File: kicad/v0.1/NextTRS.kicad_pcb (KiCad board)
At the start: 2 copper layers, 63 parts, among them J1 TRS-80 M3 Pin Header, J10 DB15_Female_HighDensity, J2 TRS-80 M1 Pin Connector, J3 TRS-80 M3 Edge Connector, J4 TRS-80 M1 Edge Connector, J5 Programmer, J6 SD_Card, J7 AudioJack3, J8 Mini-DIN-6, J9 USB_B_Micro, Q1 2N7002, Q2 2N7002, Q3 2N7002, Q4 MMBT3904, Q5 MMBT3904, SW1 SW_Push, SW2 ESP_RESET, SW3 PTRS_RESET, SW4 SW_Push, SW5 SW_DIP_x04, U1 ESP32-WROVER-B, U2 74LVC245, U3 74LVC245, U4 74LVC245, U5 74LVC245, U6 74LVC245, U7 MCP43x1

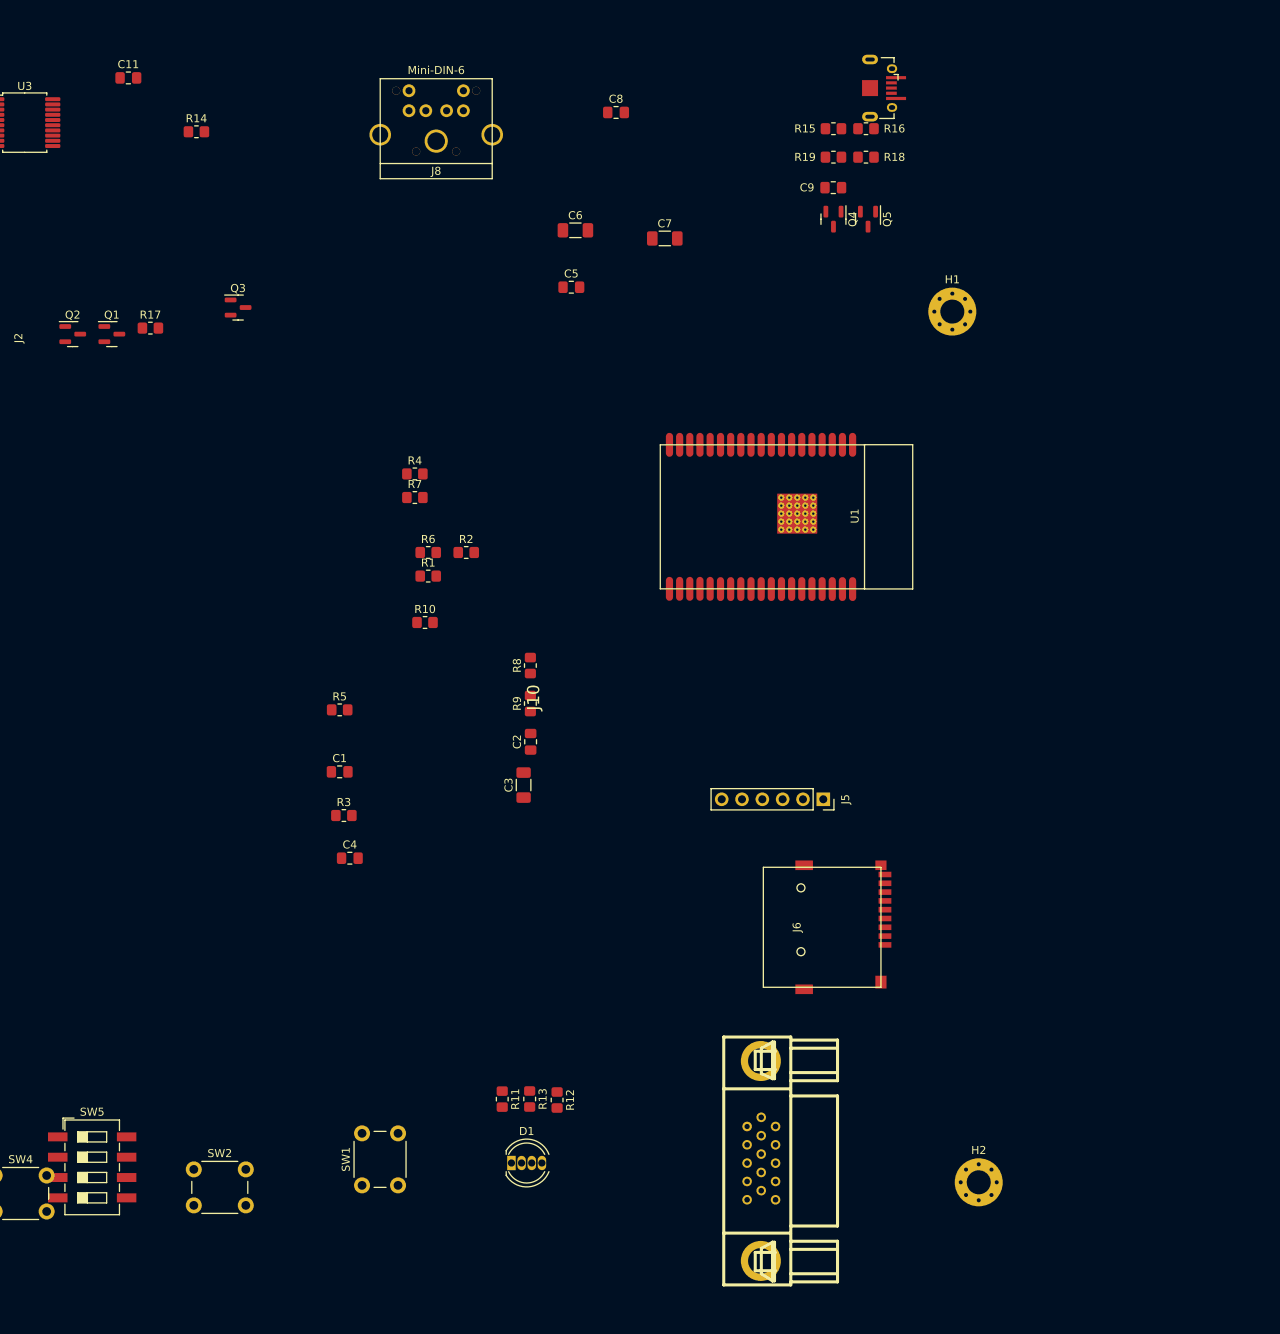
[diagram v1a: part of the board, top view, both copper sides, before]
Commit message: Add hires interface for the M3
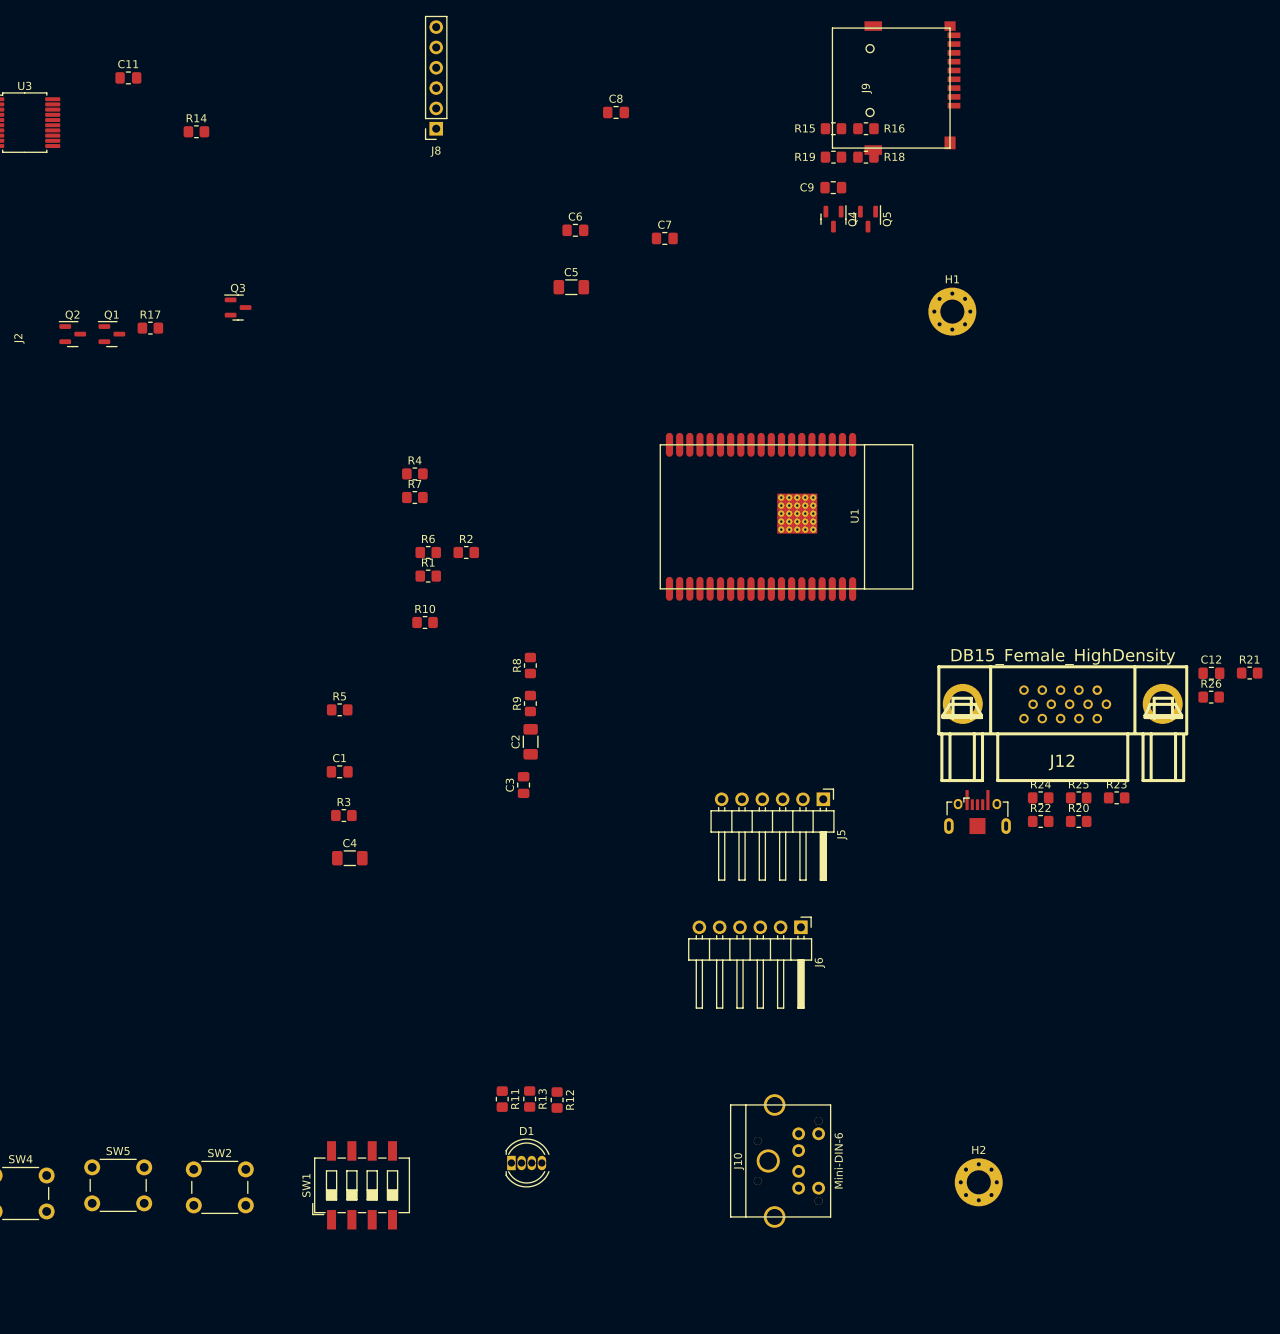
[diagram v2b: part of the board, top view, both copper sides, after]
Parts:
- added C12: 0.1uF, Capacitor_SMD:C_0805_2012Metric_Pad1.18x1.45mm_HandSolder, F.Cu at (305.8, 90.4)
- added J11: USB_B_Micro, PocketTRS_Connectors:USBmicro-B, F.Cu at (276.6, 109.5)
- added J12: DB15_Female_HighDensity, PocketTRS_Connectors:DB_15F-VGA, F.Cu at (287.2, 96.7)
- added R20: 12K, Resistor_SMD:R_0805_2012Metric_Pad1.20x1.40mm_HandSolder, F.Cu at (289.2, 108.9)
- added R21: 4K7, Resistor_SMD:R_0805_2012Metric_Pad1.20x1.40mm_HandSolder, F.Cu at (310.6, 90.4)
- added R22: 4K7, Resistor_SMD:R_0805_2012Metric_Pad1.20x1.40mm_HandSolder, F.Cu at (284.5, 108.9)
- added R23: 4K7, Resistor_SMD:R_0805_2012Metric_Pad1.20x1.40mm_HandSolder, F.Cu at (294.0, 106.0)
- added R24: 2K, Resistor_SMD:R_0805_2012Metric_Pad1.20x1.40mm_HandSolder, F.Cu at (284.5, 106.0)
- added R25: 2K, Resistor_SMD:R_0805_2012Metric_Pad1.20x1.40mm_HandSolder, F.Cu at (289.2, 106.0)
- added R26: 4K7, Resistor_SMD:R_0805_2012Metric_Pad1.20x1.40mm_HandSolder, F.Cu at (305.8, 93.4)
- C1: value 0.1uF -> 100
- C2: value 0.1uF -> 1U; footprint Capacitor_SMD:C_0805_2012Metric_Pad1.18x1.45mm_HandSolder -> Capacitor_SMD:C_1206_3216Metric_Pad1.33x1.80mm_HandSolder
- C3: value 1U -> 100N; footprint Capacitor_SMD:C_1206_3216Metric_Pad1.33x1.80mm_HandSolder -> Capacitor_SMD:C_0805_2012Metric_Pad1.18x1.45mm_HandSolder
- C4: value 100N -> 10U; footprint Capacitor_SMD:C_0805_2012Metric_Pad1.18x1.45mm_HandSolder -> Capacitor_SMD:C_1206_3216Metric_Pad1.33x1.80mm_HandSolder
- C5: value 0.1uF -> 10U; footprint Capacitor_SMD:C_0805_2012Metric_Pad1.18x1.45mm_HandSolder -> Capacitor_SMD:C_1206_3216Metric_Pad1.33x1.80mm_HandSolder
- C6, C7: value 10U -> 0.1uF; footprint Capacitor_SMD:C_1206_3216Metric_Pad1.33x1.80mm_HandSolder -> Capacitor_SMD:C_0805_2012Metric_Pad1.18x1.45mm_HandSolder
- C8: value 100N -> 0.1uF
- C9: value 0.1uF -> 100N
- J10: value DB15_Female_HighDensity -> Mini-DIN-6; footprint PocketTRS_Connectors:DB_15F-VGA -> PocketTRS_Connectors:minidin_6_ps2_pcb_mount
- J5: value Programmer -> Conn_01x06_Male; footprint Connector_PinSocket_2.54mm:PinSocket_1x06_P2.54mm_Vertical -> Connector_PinHeader_2.54mm:PinHeader_1x06_P2.54mm_Horizontal
- J6: value SD_Card -> Conn_01x06_Male; footprint PocketTRS_Connectors:TFP09-2-12B -> Connector_PinHeader_2.54mm:PinHeader_1x06_P2.54mm_Horizontal
- J8: value Mini-DIN-6 -> Programmer; footprint PocketTRS_Connectors:minidin_6_ps2_pcb_mount -> Connector_PinSocket_2.54mm:PinSocket_1x06_P2.54mm_Vertical
- J9: value USB_B_Micro -> SD_Card; footprint PocketTRS_Connectors:USBmicro-B -> PocketTRS_Connectors:TFP09-2-12B
- R10, R15, R16: value 4K7 -> 10K
- R12: value 270R -> 4K7
- R13: value 150R -> 270R
- R14: value 4K7 -> 150R
- R17, R18: value 2K -> 10K
- R19: value 4K7 -> 12K
- R4, R5: value 10K -> 4K7
- R6, R7: value 12K -> 4K7
- SW1: value SW_Push -> SW_DIP_x04; footprint Button_Switch_THT:SW_PUSH_6mm -> Button_Switch_SMD:SW_DIP_SPSTx04_Slide_6.7x11.72mm_W8.61mm_P2.54mm_LowProfile
- SW2: value ESP_RESET -> SW_Push
- SW3: value PTRS_RESET -> ESP_RESET
- SW4: value SW_Push -> PTRS_RESET
- SW5: value SW_DIP_x04 -> SW_Push; footprint Button_Switch_SMD:SW_DIP_SPSTx04_Slide_6.7x11.72mm_W8.61mm_P2.54mm_LowProfile -> Button_Switch_THT:SW_PUSH_6mm
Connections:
- C1 pad 1: GND -> VIDEO_O
- C1 pad 2: +3V3 -> GND
- C2 pad 1: GND -> CASS_IN
- C2 pad 2: +3V3 -> GND
- C3 pad 1: CASS_IN -> Net-(C3-Pad1)
- C4 pad 2: GND -> CASS_IN
- C5 pad 1: GND -> Net-(C5-Pad1)
- C5 pad 2: +3V3 -> Net-(C3-Pad1)
- C6 pad 1: Net-(C6-Pad1) -> GND
- C6 pad 2: CASS_IN -> +3V3
- C7 pad 1: Net-(C7-Pad1) -> GND
- C7 pad 2: Net-(C4-Pad1) -> +3V3
- C8 pad 1: ESP_RESET -> GND
- C8 pad 2: GND -> +3V3
- C9 pad 1: GND -> ESP_RESET
- C9 pad 2: +3V3 -> GND
- Conn1 pad 143: unconnected-(Conn1-Pad143) -> CONF_4
- Conn1 pad 147: unconnected-(Conn1-Pad147) -> CONF_3
- Conn1 pad 149: unconnected-(Conn1-Pad149) -> CONF_2
- Conn1 pad 153: unconnected-(Conn1-Pad153) -> CONF_1
- Conn1 pad 183: unconnected-(Conn1-Pad183) -> HSYNC_O
- Conn1 pad 191: unconnected-(Conn1-Pad191) -> VSYNC_O
- Conn1 pad 192: CONF_1 -> HSYNCX
- Conn1 pad 193: unconnected-(Conn1-Pad193) -> VIDEO_O
- Conn1 pad 194: CONF_2 -> VSYNCX
- Conn1 pad 198: CONF_3 -> VIDEOX
- Conn1 pad 200: CONF_4 -> unconnected-(Conn1-Pad200)
- J10 pad 1: POT_VGA_RED -> PS2_DATA
- J10 pad 2: POT_VGA_GREEN -> unconnected-(J10-Pad2)
- J10 pad 3: POT_VGA_BLUE -> GND
- J10 pad 4: unconnected-(J10-Pad4) -> +5V
- J10 pad 5: GND -> PS2_CLK
- J10 pad 6: GND -> unconnected-(J10-Pad6)
- J5 pad 1: Net-(J5-Pad1) -> GND
- J5 pad 2: Net-(J5-Pad2) -> VIDEO
- J5 pad 3: TXD0 -> GND
- J5 pad 4: RXD0 -> VSYNC
- J5 pad 5: +5V -> GND
- J5 pad 6: GND -> HSYNC
- J6 pad 1: Net-(J6-Pad1) -> GND
- J6 pad 2: CS_SD -> VIDEO_O
- J6 pad 3: MOSI -> GND
- J6 pad 4: +3.3V -> VSYNC_O
- J6 pad 5: SCK -> GND
- J6 pad 6: GND -> HSYNC_O
- J7 pad R: Net-(C6-Pad1) -> Net-(C4-Pad1)
- J7 pad T: Net-(C7-Pad1) -> Net-(C5-Pad1)
- J8 pad 1: PS2_DATA -> Net-(J8-Pad1)
- J8 pad 2: unconnected-(J8-Pad2) -> Net-(J8-Pad2)
- J8 pad 3: GND -> TXD0
- J8 pad 4: +5V -> RXD0
- J8 pad 5: PS2_CLK -> +5V
- J8 pad 6: unconnected-(J8-Pad6) -> GND
- J9 pad 1: +5V -> Net-(J9-Pad1)
- J9 pad 2: unconnected-(J9-Pad2) -> CS_SD
- J9 pad 3: unconnected-(J9-Pad3) -> MOSI
- J9 pad 4: unconnected-(J9-Pad4) -> +3.3V
- J9 pad 5: GND -> SCK
- Q4 pad 2: Net-(J5-Pad1) -> Net-(J8-Pad1)
- Q5 pad 2: Net-(J5-Pad2) -> Net-(J8-Pad2)
- R10 pad 1: +3.3V -> VIDEO
- R10 pad 2: CASS_IN -> GND
- R11 pad 1: CASS_IN -> +3.3V
- R11 pad 2: GND -> CASS_IN
- R12 pad 1: Net-(C4-Pad1) -> CASS_IN
- R12 pad 2: CASS_OUT -> GND
- R13 pad 1: Net-(C4-Pad1) -> Net-(C3-Pad1)
- R13 pad 2: GND -> CASS_OUT
- R14 pad 1: +3V3 -> Net-(C3-Pad1)
- R14 pad 2: I00 -> GND
- R15 pad 1: +3V3 -> +3.3V
- R15 pad 2: ESP_RESET -> MOSI
- R16 pad 1: +3V3 -> +3.3V
- R16 pad 2: PTRS_RESET -> Net-(J9-Pad8)
- R17 pad 1: PS2_CLK -> +3.3V
- R17 pad 2: +3.3V -> CS_SD
- R18 pad 1: PS2_DATA -> +3.3V
- R18 pad 2: +3.3V -> Net-(J9-Pad1)
- R19 pad 1: +3.3V -> Net-(Q4-Pad1)
- R19 pad 2: BUTTON -> Net-(J8-Pad2)
- R4 pad 2: MOSI -> CONF_1
- R5 pad 2: Net-(J6-Pad8) -> CONF_2
- R6 pad 1: Net-(Q4-Pad1) -> +3.3V
- R6 pad 2: Net-(J5-Pad2) -> CONF_3
- R7 pad 1: Net-(Q5-Pad1) -> +3.3V
- R7 pad 2: Net-(J5-Pad1) -> CONF_4
- R8 pad 1: +3.3V -> HSYNC
- R8 pad 2: CS_SD -> GND
- R9 pad 1: +3.3V -> VSYNC
- R9 pad 2: Net-(J6-Pad1) -> GND
- SW1 pad 2: BUTTON -> GND
- SW2 pad 1: ESP_RESET -> GND
- SW2 pad 2: GND -> BUTTON
- SW3 pad 1: GND -> ESP_RESET
- SW3 pad 2: PTRS_RESET -> GND
- SW4 pad 2: BUTTON -> PTRS_RESET
- SW5 pad 2: GND -> BUTTON
- U5 pad 13: unconnected-(U5-Pad13) -> VIDEOX
- U5 pad 14: unconnected-(U5-Pad14) -> VSYNCX
- U5 pad 15: unconnected-(U5-Pad15) -> HSYNCX
- U5 pad 5: unconnected-(U5-Pad5) -> HSYNC
- U5 pad 6: unconnected-(U5-Pad6) -> VSYNC
- U5 pad 7: unconnected-(U5-Pad7) -> VIDEO

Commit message: Add HDMI connector
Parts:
- removed SW4: PTRS_RESET, Button_Switch_THT:SW_PUSH_6mm
- removed SW5: SW_Push, Button_Switch_THT:SW_PUSH_6mm
- removed U7: MCP43x1, Package_SO:TSSOP-20_4.4x6.5mm_P0.65mm
- added C13: 100N, Capacitor_SMD:C_0805_2012Metric_Pad1.18x1.45mm_HandSolder, F.Cu at (78.6, 181.7)
- added C14: 10U, Capacitor_SMD:C_1206_3216Metric_Pad1.33x1.80mm_HandSolder, F.Cu at (79.2, 175.5)
- added C15: 10U, Capacitor_SMD:C_1206_3216Metric_Pad1.33x1.80mm_HandSolder, F.Cu at (79.2, 172.2)
- added C16: 0.1uF, Capacitor_SMD:C_0805_2012Metric_Pad1.18x1.45mm_HandSolder, F.Cu at (84.6, 175.3)
- added C17: 100N, Capacitor_SMD:C_0805_2012Metric_Pad1.18x1.45mm_HandSolder, F.Cu at (78.6, 178.7)
- added C18: 0.1uF, Capacitor_SMD:C_0805_2012Metric_Pad1.18x1.45mm_HandSolder, F.Cu at (83.4, 178.7)
- added C19: 0.1uF, Capacitor_SMD:C_0805_2012Metric_Pad1.18x1.45mm_HandSolder, F.Cu at (90.6, 172.0)
- added R27: 4K7, Resistor_SMD:R_0805_2012Metric_Pad1.20x1.40mm_HandSolder, F.Cu at (35.2, 127.7)
- added R28: 4K7, Resistor_SMD:R_0805_2012Metric_Pad1.20x1.40mm_HandSolder, F.Cu at (33.0, 127.7)
- added R29: 4K7, Resistor_SMD:R_0805_2012Metric_Pad1.20x1.40mm_HandSolder, F.Cu at (30.9, 127.7)
- added R30: 4K7, Resistor_SMD:R_0805_2012Metric_Pad1.20x1.40mm_HandSolder, F.Cu at (88.1, 181.7)
- added R31: 2K, Resistor_SMD:R_0805_2012Metric_Pad1.20x1.40mm_HandSolder, F.Cu at (95.4, 172.0)
- added R32: 2K, Resistor_SMD:R_0805_2012Metric_Pad1.20x1.40mm_HandSolder, F.Cu at (88.2, 178.3)
- added R33: 4K7, Resistor_SMD:R_0805_2012Metric_Pad1.20x1.40mm_HandSolder, F.Cu at (94.1, 175.0)
- added R34: 4K7, Resistor_SMD:R_0805_2012Metric_Pad1.20x1.40mm_HandSolder, F.Cu at (94.1, 177.9)
- added R35: 4K7, Resistor_SMD:R_0805_2012Metric_Pad1.20x1.40mm_HandSolder, F.Cu at (89.4, 175.3)
- added R36: 4K7, Resistor_SMD:R_0805_2012Metric_Pad1.20x1.40mm_HandSolder, F.Cu at (83.4, 181.7)
- C1: value 100 -> 100n
- C12: value 0.1uF -> 1U; footprint Capacitor_SMD:C_0805_2012Metric_Pad1.18x1.45mm_HandSolder -> Capacitor_SMD:C_1206_3216Metric_Pad1.33x1.80mm_HandSolder
- C2: value 1U -> 100n; footprint Capacitor_SMD:C_1206_3216Metric_Pad1.33x1.80mm_HandSolder -> Capacitor_SMD:C_0805_2012Metric_Pad1.18x1.45mm_HandSolder
- C3: value 100N -> 100n
- C4, C5: value 10U -> 100n; footprint Capacitor_SMD:C_1206_3216Metric_Pad1.33x1.80mm_HandSolder -> Capacitor_SMD:C_0805_2012Metric_Pad1.18x1.45mm_HandSolder
- C6, C7, C8: value 0.1uF -> 100n
- C9: value 100N -> 100
- D1: value LED_RCBG -> LED_RKBG
- J1: footprint Connector_PinSocket_2.54mm:PinSocket_2x25_P2.54mm_Vertical -> Connector_PinHeader_2.54mm:PinHeader_2x25_P2.54mm_Vertical
- J10: value Mini-DIN-6 -> AudioJack3; footprint PocketTRS_Connectors:minidin_6_ps2_pcb_mount -> PocketTRS_Connectors:Jack_3.5mm_CUI_SJ1-3535NG_Horizontal_CircularHoles
- J11: value USB_B_Micro -> Mini-DIN-6; footprint PocketTRS_Connectors:USBmicro-B -> PocketTRS_Connectors:minidin_6_ps2_pcb_mount
- J12: value DB15_Female_HighDensity -> USB_B_Micro; footprint PocketTRS_Connectors:DB_15F-VGA -> PocketTRS_Connectors:USBmicro-B
- J2: footprint Connector_PinSocket_2.54mm:PinSocket_2x20_P2.54mm_Vertical -> Connector_PinHeader_2.54mm:PinHeader_2x20_P2.54mm_Vertical
- J7: value AudioJack3 -> HDMI_A; footprint PocketTRS_Connectors:Jack_3.5mm_CUI_SJ1-3535NG_Horizontal_CircularHoles -> Connector_HDMI:HDMI_A_Molex_208658-1001_Horizontal
- Q1, Q2: value 2N7002 -> MMBT3904
- Q4, Q5: value MMBT3904 -> 2N7002
- R10, R8, R9: value 10K -> 50
- R11, R4, R5, R6, R7: value 4K7 -> 50
- R12: value 4K7 -> 10K
- R13: value 270R -> 10K
- R14: value 150R -> 10K
- R23: value 4K7 -> 270R
- R24: value 2K -> 150R
- R25: value 2K -> 4K7
- SW1: value SW_DIP_x04 -> ESP_RESET; footprint Button_Switch_SMD:SW_DIP_SPSTx04_Slide_6.7x11.72mm_W8.61mm_P2.54mm_LowProfile -> Button_Switch_THT:SW_PUSH_6mm
- SW2: value SW_Push -> PTRS_RESET
- SW3: value ESP_RESET -> SW_DIP_x04; footprint Button_Switch_THT:SW_PUSH_6mm -> Button_Switch_SMD:SW_DIP_SPSTx04_Slide_6.7x11.72mm_W8.61mm_P2.54mm_LowProfile
- moved C1 241.8 mm to (-42.1, 139.5)
- moved C12 235.3 mm to (85.2, 172.2)
- moved J1 184.9 mm to (-4.52, 46.8), turned to 90 degrees
- moved U3 165.2 mm to (5.54, 86.5)
- moved J3 159.5 mm to (34.2, 35.0), turned to 180 degrees
- moved U2 139.5 mm to (5.23, 97.4)
- moved U4 108.2 mm to (32.6, 88.1)
- moved J6 107.2 mm to (155.3, 162.9)
- moved R17 102.1 mm to (274.2, 32.7), turned to 90 degrees
- moved J5 100.6 mm to (174.1, 162.8)
- moved R8 85.9 mm to (136.1, 74.3)
- moved R9 84.6 mm to (138.5, 74.3)
- moved U1 83.2 mm to (188.5, 110.1)
- moved R10 79.9 mm to (171.5, 155.4), turned to 90 degrees
- moved C2 79.9 mm to (144.3, 75.9)
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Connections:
- C1 pad 1: VIDEO_O -> HDMI_TX2_P
- C1 pad 2: GND -> Net-(J7-Pad1)
- C12 pad 1: GND -> CASS_IN
- C12 pad 2: +3V3 -> GND
- C2 pad 1: CASS_IN -> HDMI_TX2_N
- C2 pad 2: GND -> Net-(J7-Pad3)
- C3 pad 1: Net-(C3-Pad1) -> HDMI_TX1_P
- C3 pad 2: GND -> Net-(J7-Pad4)
- C4 pad 1: Net-(C4-Pad1) -> HDMI_TX1_N
- C4 pad 2: CASS_IN -> Net-(J7-Pad6)
- C5 pad 1: Net-(C5-Pad1) -> HDMI_TX0_P
- C5 pad 2: Net-(C3-Pad1) -> Net-(J7-Pad7)
- C6 pad 1: GND -> HDMI_TX0_N
- C6 pad 2: +3V3 -> Net-(J7-Pad9)
- C7 pad 1: GND -> HDMI_TXC_P
- C7 pad 2: +3V3 -> Net-(J7-Pad10)
- C8 pad 1: GND -> HDMI_TXC_N
- C8 pad 2: +3V3 -> Net-(J7-Pad12)
- C9 pad 1: ESP_RESET -> VIDEO_O
- Conn1 pad 101: DBUS_DIR -> _D2
- Conn1 pad 103: unconnected-(Conn1-Pad103) -> _D1
- Conn1 pad 107: _RAS_N -> _D0
- Conn1 pad 109: _OUT_N -> unconnected-(Conn1-Pad109)
- Conn1 pad 113: _IN_N -> unconnected-(Conn1-Pad113)
- Conn1 pad 115: _RD_N -> unconnected-(Conn1-Pad115)
- Conn1 pad 119: _WR_N -> unconnected-(Conn1-Pad119)
- Conn1 pad 121: _IOREQ_N -> unconnected-(Conn1-Pad121)
- Conn1 pad 123: _M1_N -> unconnected-(Conn1-Pad123)
- Conn1 pad 125: _RESET_N -> unconnected-(Conn1-Pad125)
- Conn1 pad 130: unconnected-(Conn1-Pad130) -> DONE
- Conn1 pad 135: unconnected-(Conn1-Pad135) -> CASS_OUT
- Conn1 pad 140: EXTIOSEL -> unconnected-(Conn1-Pad140)
- Conn1 pad 142: WAIT -> unconnected-(Conn1-Pad142)
- Conn1 pad 146: INT -> unconnected-(Conn1-Pad146)
- Conn1 pad 148: CTRL_DIR -> unconnected-(Conn1-Pad148)
- Conn1 pad 152: CTRL_EN -> unconnected-(Conn1-Pad152)
- Conn1 pad 154: CTRL1_EN -> EXTIOSEL
- Conn1 pad 176: EXTIOSEL_OUT_N -> WAIT
- Conn1 pad 177: unconnected-(Conn1-Pad177) -> HSYNC_O
- Conn1 pad 180: WAIT_OUT_N -> INT
- Conn1 pad 182: INT_OUT_N -> CTRL1_EN
- Conn1 pad 183: HSYNC_O -> VSYNC_O
- Conn1 pad 186: unconnected-(Conn1-Pad186) -> EXTIOSEL_IN_N
- Conn1 pad 191: VSYNC_O -> VIDEO_O
- Conn1 pad 192: HSYNCX -> WAIT_IN_N
- Conn1 pad 193: VIDEO_O -> VIDEOX
- Conn1 pad 194: VSYNCX -> INT_IN_N
- Conn1 pad 198: VIDEOX -> HSYNCX
- Conn1 pad 200: unconnected-(Conn1-Pad200) -> VSYNCX
- Conn1 pad 26: unconnected-(Conn1-Pad26) -> GND
- Conn1 pad 27: _A0 -> CTRL_DIR
- Conn1 pad 28: VGA_RED -> ABUS_DIR_N
- Conn1 pad 29: _A1 -> CTRL_EN
- Conn1 pad 30: VGA_GREEN -> _A10
- Conn1 pad 33: _A2 -> _RD_N
- Conn1 pad 34: VGA_BLUE -> _A12
- Conn1 pad 35: _A3 -> _WR_N
- Conn1 pad 36: VGA_VSYNC -> _A13
- Conn1 pad 39: _A4 -> _RAS_N
- Conn1 pad 40: VGA_HSYNC -> _A15
- Conn1 pad 41: _A5 -> _IOREQ_N
- Conn1 pad 42: CS_FPGA -> _A14
- Conn1 pad 44: SCK -> _A11
- Conn1 pad 45: _A6 -> _M1_N
- Conn1 pad 46: MISO -> _A8
- Conn1 pad 47: _A7 -> _RESET_N
- Conn1 pad 50: MOSI -> HDMI_TX2_N
- Conn1 pad 51: _A8 -> _OUT_N
- Conn1 pad 52: ESP_S0 -> HDMI_TX2_P
- Conn1 pad 53: _A9 -> _IN_N
- Conn1 pad 56: ESP_S1 -> HDMI_TX1_N
- Conn1 pad 57: _A10 -> ABUS_DIR
- Conn1 pad 58: ESP_S2 -> HDMI_TX1_P
- Conn1 pad 59: _A11 -> ABUS_EN
- Conn1 pad 62: ESP_S3 -> HDMI_TX0_N
- Conn1 pad 63: _A12 -> _A7
- Conn1 pad 64: REQ -> HDMI_TX0_P
- Conn1 pad 65: _A13 -> _A6
- Conn1 pad 67: _A14 -> _A5
- Conn1 pad 68: DONE -> HDMI_TXC_P
- Conn1 pad 69: _A15 -> _A4
- Conn1 pad 70: CASS_OUT -> HDMI_TXC_N
- Conn1 pad 73: ABUS_EN -> _A3
- Conn1 pad 74: unconnected-(Conn1-Pad74) -> _A9
- Conn1 pad 75: ABUS_DIR -> _A2
- Conn1 pad 76: unconnected-(Conn1-Pad76) -> CS_FPGA
- Conn1 pad 77: _D0 -> _A1
- Conn1 pad 78: unconnected-(Conn1-Pad78) -> SCK
- Conn1 pad 79: _D1 -> _A0
- Conn1 pad 80: unconnected-(Conn1-Pad80) -> MISO
- Conn1 pad 81: _D2 -> DBUS_DIR
- Conn1 pad 83: _D3 -> DBUS_EN
- Conn1 pad 84: unconnected-(Conn1-Pad84) -> MOSI
- Conn1 pad 85: _D4 -> _D7
- Conn1 pad 86: unconnected-(Conn1-Pad86) -> ESP_S0
- Conn1 pad 89: _D5 -> _D6
- Conn1 pad 90: unconnected-(Conn1-Pad90) -> ESP_S1
- Conn1 pad 91: _D6 -> _D5
- Conn1 pad 92: unconnected-(Conn1-Pad92) -> ESP_S2
- Conn1 pad 95: _D7 -> _D4
- Conn1 pad 96: unconnected-(Conn1-Pad96) -> ESP_S3
- Conn1 pad 97: DBUS_EN -> _D3
- Conn1 pad 98: unconnected-(Conn1-Pad98) -> REQ
- J11 pad 1: +5V -> PS2_DATA
- J11 pad 3: unconnected-(J11-Pad3) -> GND
- J11 pad 4: unconnected-(J11-Pad4) -> +5V
- J11 pad 5: GND -> PS2_CLK
- J12 pad 1: POT_VGA_RED -> +5V
- J12 pad 2: POT_VGA_GREEN -> unconnected-(J12-Pad2)
- J12 pad 3: POT_VGA_BLUE -> unconnected-(J12-Pad3)
- Q1 pad 1: INT -> Net-(Q1-Pad1)
- Q1 pad 2: GND -> Net-(J8-Pad1)
- Q1 pad 3: INT_N -> ESP_RESET
- Q2 pad 1: WAIT -> Net-(Q2-Pad1)
- Q2 pad 2: GND -> Net-(J8-Pad2)
- Q2 pad 3: WAIT_N -> I00
- Q3 pad 1: EXTIOSEL -> INT
- Q3 pad 3: EXTIOSEL_N -> INT_N
- Q4 pad 1: Net-(Q4-Pad1) -> WAIT
- Q4 pad 2: Net-(J8-Pad1) -> GND
- Q4 pad 3: ESP_RESET -> WAIT_N
- Q5 pad 1: Net-(Q5-Pad1) -> EXTIOSEL
- Q5 pad 2: Net-(J8-Pad2) -> GND
- Q5 pad 3: I00 -> EXTIOSEL_N
- R10 pad 1: VIDEO -> +3.3V
- R10 pad 2: GND -> HDMI_TXC_P
- R11 pad 2: CASS_IN -> HDMI_TXC_N
- R12 pad 1: CASS_IN -> HSYNC
- R13 pad 1: Net-(C3-Pad1) -> VSYNC
- R13 pad 2: CASS_OUT -> GND
- R14 pad 1: Net-(C3-Pad1) -> VIDEO
- R19 pad 1: Net-(Q4-Pad1) -> Net-(Q1-Pad1)
- R20 pad 1: Net-(Q5-Pad1) -> Net-(Q2-Pad1)
- R21 pad 1: +3V3 -> +3.3V
- R21 pad 2: I00 -> CASS_IN
- R22 pad 1: +3V3 -> CASS_IN
- R22 pad 2: ESP_RESET -> GND
- R23 pad 1: +3V3 -> Net-(C13-Pad1)
- R23 pad 2: PTRS_RESET -> CASS_OUT
- R24 pad 1: PS2_CLK -> Net-(C13-Pad1)
- R24 pad 2: +3.3V -> GND
- R25 pad 1: PS2_DATA -> +3.3V
- R25 pad 2: +3.3V -> I00
- R26 pad 1: +3.3V -> +3V3
- R26 pad 2: BUTTON -> INT_IN_N
- R4 pad 2: CONF_1 -> HDMI_TX2_P
- R5 pad 2: CONF_2 -> HDMI_TX2_N
- R6 pad 2: CONF_3 -> HDMI_TX1_P
- R7 pad 2: CONF_4 -> HDMI_TX1_N
- R8 pad 1: HSYNC -> +3.3V
- R8 pad 2: GND -> HDMI_TX0_P
- R9 pad 1: VSYNC -> +3.3V
- R9 pad 2: GND -> HDMI_TX0_N
- SW1 pad 1: GND -> ESP_RESET
- SW3 pad 1: ESP_RESET -> GND
- U1 pad 26: CS43x1 -> unconnected-(U1-Pad26)
- U1 pad 5: BUTTON -> unconnected-(U1-Pad5)
- U1 pad 7: PTRS_RESET -> BUTTON
- U2 pad 11: _A7 -> _A0
- U2 pad 12: _A6 -> _A1
- U2 pad 13: _A5 -> _A2
- U2 pad 14: _A4 -> _A3
- U2 pad 15: _A3 -> _A4
- U2 pad 16: _A2 -> _A5
- U2 pad 17: _A1 -> _A6
- U2 pad 18: _A0 -> _A7
- U2 pad 2: A0 -> A7
- U2 pad 3: A1 -> A6
- U2 pad 4: A2 -> A5
- U2 pad 5: A3 -> A4
- U2 pad 6: A4 -> A3
- U2 pad 7: A5 -> A2
- U2 pad 8: A6 -> A1
- U2 pad 9: A7 -> A0
- U3 pad 11: _RESET_N -> _IN_N
- U3 pad 12: _M1_N -> _OUT_N
- U3 pad 13: _IOREQ_N -> _RESET_N
- U3 pad 14: _WR_N -> _M1_N
- U3 pad 15: _RD_N -> _IOREQ_N
- U3 pad 16: _IN_N -> _RAS_N
- U3 pad 17: _OUT_N -> _WR_N
- U3 pad 18: _RAS_N -> _RD_N
- U3 pad 2: RAS_N -> RD_N
- U3 pad 3: OUT_N -> WR_N
- U3 pad 4: IN_N -> RAS_N
- U3 pad 5: RD_N -> IOREQ_N
- U3 pad 6: WR_N -> M1_N
- U3 pad 7: IOREQ_N -> RESET_N
- U3 pad 8: M1_N -> OUT_N
- U3 pad 9: RESET_N -> IN_N
- U4 pad 1: ABUS_DIR -> ABUS_DIR_N
- U4 pad 11: _A15 -> A9
- U4 pad 12: _A14 -> A8
- U4 pad 13: _A13 -> A11
- U4 pad 14: _A12 -> A14
- U4 pad 15: _A11 -> A15
- U4 pad 16: _A10 -> A13
- U4 pad 17: _A9 -> A12
- U4 pad 18: _A8 -> A10
- U4 pad 2: A8 -> _A10
- U4 pad 3: A9 -> _A12
- U4 pad 4: A10 -> _A13
- U4 pad 5: A11 -> _A15
- U4 pad 6: A12 -> _A14
- U4 pad 7: A13 -> _A11
- U4 pad 8: A14 -> _A8
- U4 pad 9: A15 -> _A9
- U5 pad 1: +3V3 -> GND
- U5 pad 2: EXTIOSEL_OUT_N -> EXTIOSEL_IN_N
- U5 pad 3: WAIT_OUT_N -> WAIT_IN_N
- U5 pad 4: INT_OUT_N -> INT_IN_N
- U6 pad 11: _D7 -> _D0
- U6 pad 12: _D6 -> _D1
- U6 pad 13: _D5 -> _D2
- U6 pad 14: _D4 -> _D3
- U6 pad 15: _D3 -> _D4
- U6 pad 16: _D2 -> _D5
- U6 pad 17: _D1 -> _D6
- U6 pad 18: _D0 -> _D7
- U6 pad 2: D0 -> D7
- U6 pad 3: D1 -> D6
- U6 pad 4: D2 -> D5
- U6 pad 5: D3 -> D4
- U6 pad 6: D4 -> D3
- U6 pad 7: D5 -> D2
- U6 pad 8: D6 -> D1
- U6 pad 9: D7 -> D0

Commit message: Move LED to FPGA. Add JTAG interface
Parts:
- SW2: value PTRS_RESET -> PTRS_RESET/STATUS
- moved J12 272.2 mm to (15.6, 79.2), turned to -90 degrees
- moved H1 248.1 mm to (25.8, 60.5)
- moved R26 239.4 mm to (70.8, 139.0)
- moved C9 235.4 mm to (61.6, 158.6), turned to 0 degrees
- moved R27 228.9 mm to (256.3, 68.7), turned to 0 degrees
- moved H3 223.5 mm to (161.8, 169.0)
- moved SW2 214.1 mm to (24.0, 142.9)
- moved C17 205.1 mm to (246.3, 60.7)
- moved C1 187.5 mm to (139.4, 92.8)
- moved Q5 179.8 mm to (88.5, 77.4), turned to 0 degrees
- moved SW3 177.5 mm to (27.1, 132.3)
- moved SW1 175.8 mm to (23.8, 153.6), turned to 0 degrees
- moved R21 172.9 mm to (148.0, 149.3)
- moved R14 166.2 mm to (82.0, 157.8)
- moved R23 160.2 mm to (141.1, 153.9)
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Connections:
- C1 pad 2: Net-(J7-Pad1) -> Net-(C1-Pad2)
- C2 pad 2: Net-(J7-Pad3) -> Net-(C2-Pad2)
- C3 pad 2: Net-(J7-Pad4) -> Net-(C3-Pad2)
- C4 pad 2: Net-(J7-Pad6) -> Net-(C4-Pad2)
- C5 pad 2: Net-(J7-Pad7) -> Net-(C5-Pad2)
- C6 pad 2: Net-(J7-Pad9) -> Net-(C6-Pad2)
- C7 pad 2: Net-(J7-Pad10) -> Net-(C7-Pad2)
- C8 pad 2: Net-(J7-Pad12) -> Net-(C8-Pad2)
- Conn1 pad 123: unconnected-(Conn1-Pad123) -> CONF_4
- Conn1 pad 125: unconnected-(Conn1-Pad125) -> CONF_3
- Conn1 pad 129: unconnected-(Conn1-Pad129) -> CONF_2
- Conn1 pad 131: unconnected-(Conn1-Pad131) -> CONF_1
- Conn1 pad 140: unconnected-(Conn1-Pad140) -> LED_GREEN
- Conn1 pad 142: unconnected-(Conn1-Pad142) -> LED_BLUE
- Conn1 pad 143: CONF_4 -> JTAG_TMS
- Conn1 pad 146: unconnected-(Conn1-Pad146) -> LED_RED
- Conn1 pad 147: CONF_3 -> RXD0
- Conn1 pad 149: CONF_2 -> JTAG_TCK
- Conn1 pad 153: CONF_1 -> TXD0
- J7 pad 1: Net-(J7-Pad1) -> Net-(C1-Pad2)
- J7 pad 10: Net-(J7-Pad10) -> Net-(C7-Pad2)
- J7 pad 12: Net-(J7-Pad12) -> Net-(C8-Pad2)
- J7 pad 3: Net-(J7-Pad3) -> Net-(C2-Pad2)
- J7 pad 4: Net-(J7-Pad4) -> Net-(C3-Pad2)
- J7 pad 6: Net-(J7-Pad6) -> Net-(C4-Pad2)
- J7 pad 7: Net-(J7-Pad7) -> Net-(C5-Pad2)
- J7 pad 9: Net-(J7-Pad9) -> Net-(C6-Pad2)
- R10 pad 2: HDMI_TXC_P -> Net-(C7-Pad2)
- R11 pad 2: HDMI_TXC_N -> Net-(C8-Pad2)
- R4 pad 2: HDMI_TX2_P -> Net-(C1-Pad2)
- R5 pad 2: HDMI_TX2_N -> Net-(C2-Pad2)
- R6 pad 2: HDMI_TX1_P -> Net-(C3-Pad2)
- R7 pad 2: HDMI_TX1_N -> Net-(C4-Pad2)
- R8 pad 2: HDMI_TX0_P -> Net-(C5-Pad2)
- R9 pad 2: HDMI_TX0_N -> Net-(C6-Pad2)
- U1 pad 12: LED_RED -> unconnected-(U1-Pad12)
- U1 pad 29: LED_BLUE -> JTAG_TMS
- U1 pad 37: LED_GREEN -> JTAG_TCK
